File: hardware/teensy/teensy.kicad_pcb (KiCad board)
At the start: 2 copper layers, 215.9 x 152.4 mm, 99 parts, among them J4 CONN_083.5MM-8, J5 CONN_083.5MM-8, J6 CONN_083.5MM-8, J7 CONN_083.5MM-8, J8 CONN_023.5MM, J9 CONN_023.5MM

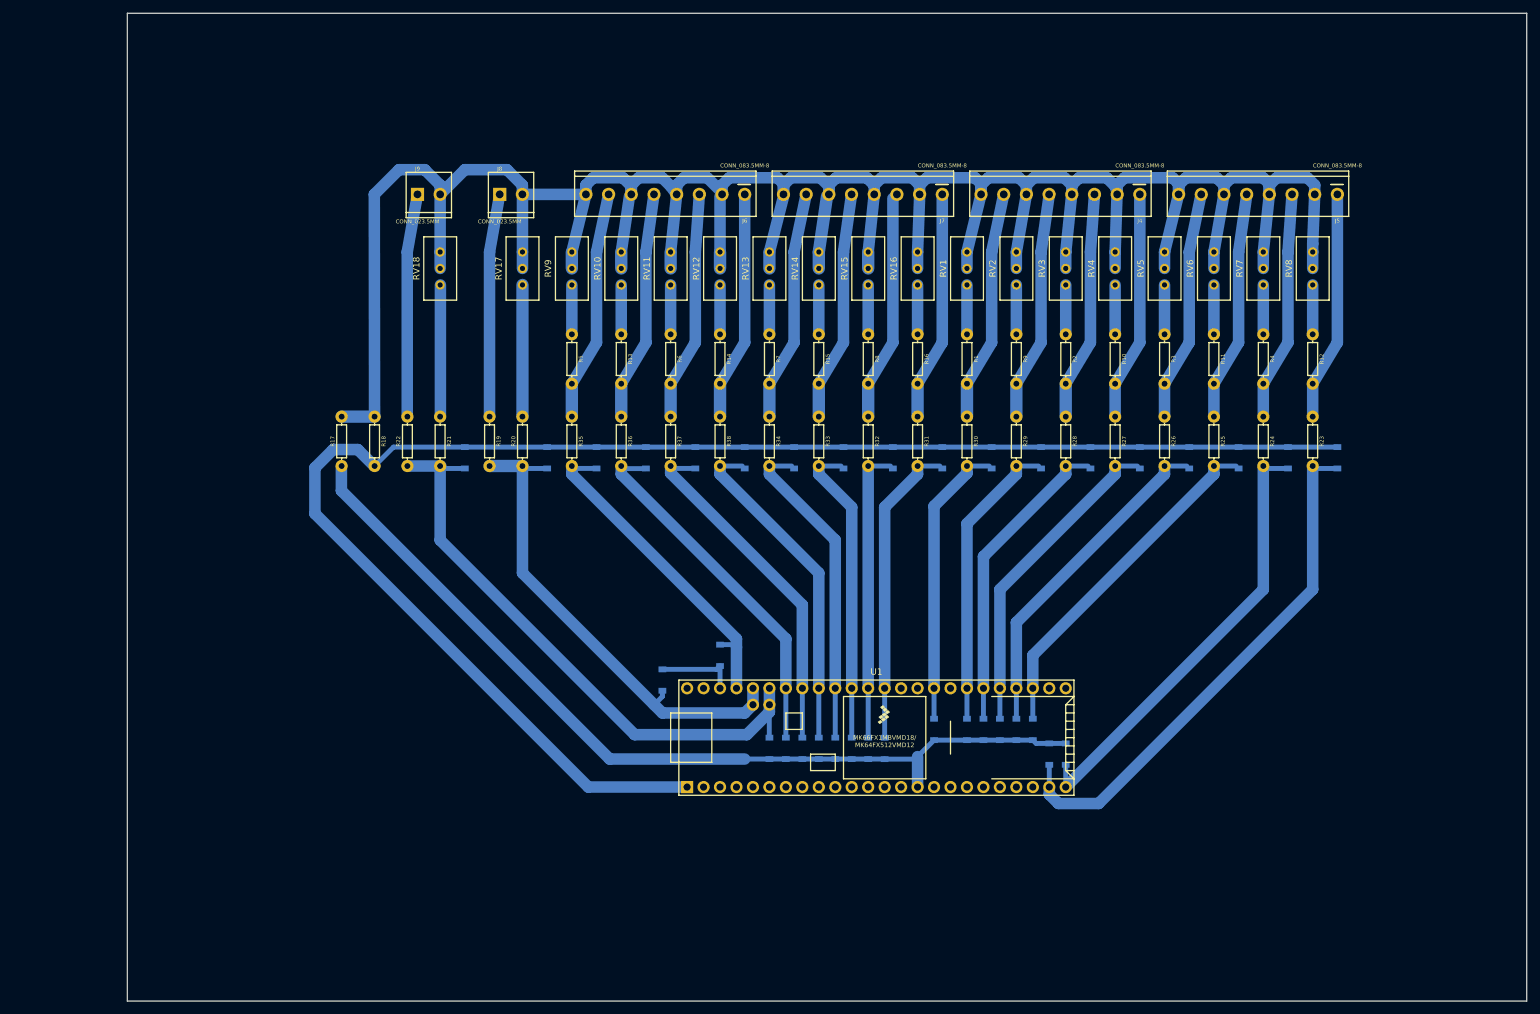
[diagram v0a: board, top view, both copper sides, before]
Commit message: got outline working
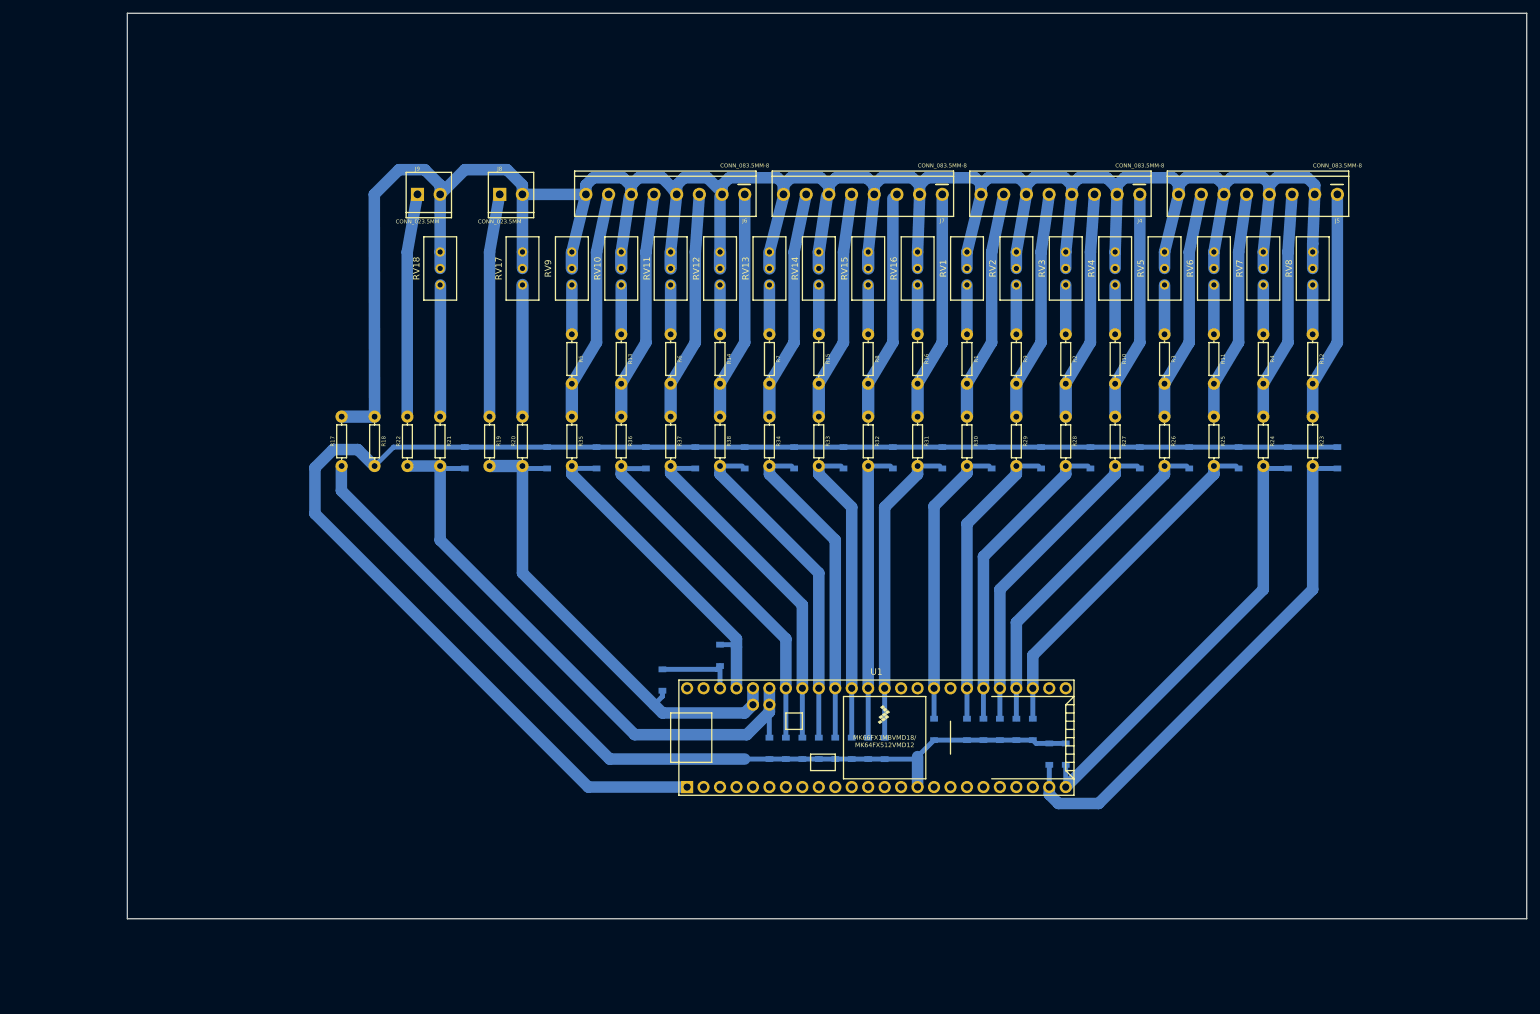
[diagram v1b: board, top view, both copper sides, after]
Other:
- board size 215.9 x 152.4 mm -> 215.9 x 139.7 mm
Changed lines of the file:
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@@
   (general
     (thickness 1.6)
-    (drawings 1)
+    (drawings 4)
     (tracks 348)
     (modules 99)
@@
       (sketchpadsonfab false)
       (subtractmaskfromsilk false)
-      (outputformat 3)
+      (outputformat 1)
       (mirror false)
       (drillshape 0)
@@
     )
   )
-  (gr_rect (start 38.1 25.4) (end 254 177.8) (layer "Edge.Cuts") (width 0.1))
+  (gr_line (start 254 25.4) (end 254 165.1) (layer "Edge.Cuts") (width 0.1))
+  (gr_line (start 38.1 25.4) (end 254 25.4) (layer "Edge.Cuts") (width 0.1))
+  (gr_line (start 38.1 165.1) (end 38.1 25.4) (layer "Edge.Cuts") (width 0.1))
+  (gr_line (start 254 165.1) (end 38.1 165.1) (layer "Edge.Cuts") (width 0.1))
   (segment (start 82.86242 53.34) (end 81.28 62.23) (width 1.778) (layer "B.Cu") (net 45))
   (segment (start 81.28 62.23) (end 81.28 87.602466) (width 1.778) (layer "B.Cu") (net 45))

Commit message: 2.54 rather than 3.5mm screws, now fits in 3x5
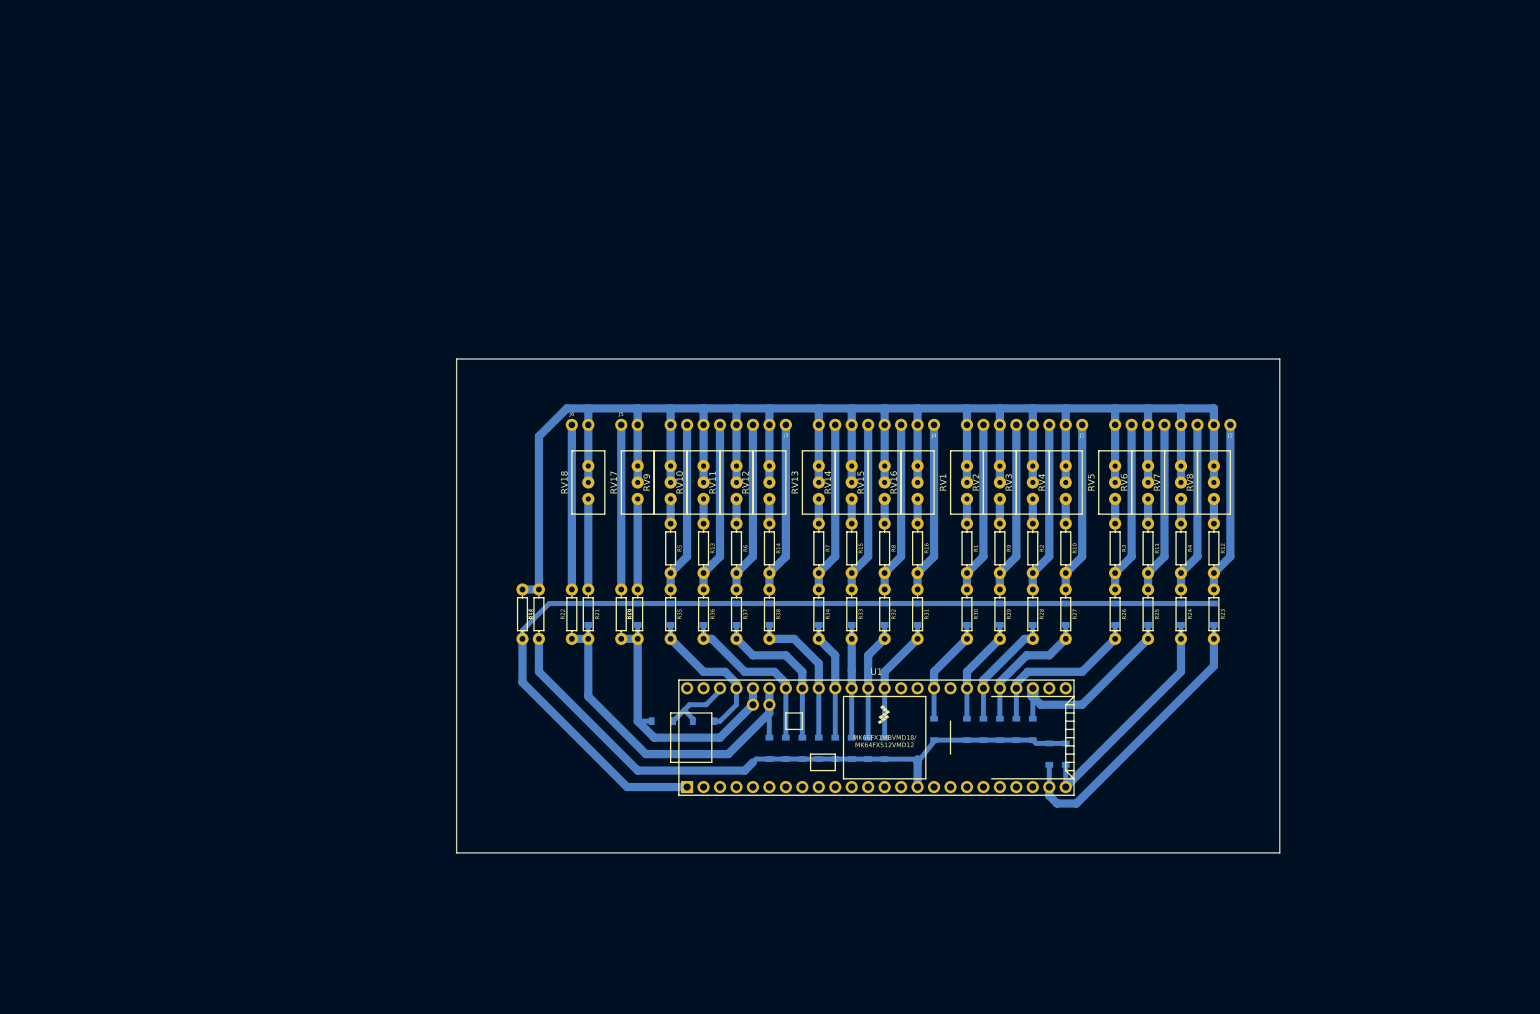
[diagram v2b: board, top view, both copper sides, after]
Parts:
- removed J7: CONN_083.5MM-8, Connectors:SCREWTERMINAL-3.5MM-8
- removed J8, J9: CONN_023.5MM, Connectors:SCREWTERMINAL-3.5MM-2
- added J1: CONN_08NO_SILK_FEMALE_PTH, Connectors:1X08_NO_SILK, F.Cu at (185.4, 88.9)
- added J2: CONN_08NO_SILK_FEMALE_PTH, Connectors:1X08_NO_SILK, F.Cu at (208.3, 88.9)
- added J3: CONN_08NO_SILK_FEMALE_PTH, Connectors:1X08_NO_SILK, F.Cu at (139.7, 88.9)
- J4: value CONN_083.5MM-8 -> CONN_08NO_SILK_FEMALE_PTH; footprint Connectors:SCREWTERMINAL-3.5MM-8 -> Connectors:1X08_NO_SILK
- J5, J6: value CONN_083.5MM-8 -> CONN_02; footprint Connectors:SCREWTERMINAL-3.5MM-8 -> Connectors:1X02_NO_SILK
- moved J5 116.1 mm to (114.3, 88.9), turned to 0 degrees
- moved J4 47.7 mm to (162.6, 88.9)
- moved J6 44.4 mm to (106.7, 88.9), turned to 0 degrees
- moved R17 40.5 mm to (101.6, 118.1)
- moved RV18 40.2 mm to (109.2, 95.2)
- moved RV17 37.5 mm to (116.8, 95.2)
- moved R22 36.8 mm to (106.7, 118.1)
- moved RV9 36.4 mm to (121.9, 95.2)
- moved RV8 36.4 mm to (205.7, 95.2)
- moved RV10 35.4 mm to (127.0, 95.2)
- moved RV7 35.4 mm to (200.7, 95.2)
- moved R21 35.1 mm to (109.2, 118.1)
- moved R18 35.1 mm to (99.1, 118.1)
- moved RV11 34.5 mm to (132.1, 95.2)
- moved RV6 34.5 mm to (195.6, 95.2)
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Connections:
- J4 pad 1: /ct13 -> /ct1
- J4 pad 3: /ct14 -> /ct2
- J4 pad 5: /ct15 -> /ct3
- J4 pad 7: /ct16 -> /ct4
- J5 pad 1: /ct9 -> /L2
- J6 pad 1: /ct5 -> /L1
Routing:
- net /CT_BIAS: track 445.6 -> 337.8 mm
- net /GND: track 243.1 -> 148.5 mm
- net /3.3V: track 138.7 -> 99.5 mm
- net /A11_A7: track 93.4 -> 55.4 mm
- net /A12: track 81.9 -> 45.9 mm
- net /A13: track 69.0 -> 35.9 mm
- net /A10_A8: track 75.3 -> 43.0 mm
- net /A3: track 49.5 -> 18.5 mm
- net /A2: track 47.4 -> 17.4 mm
- net /A6: track 55.8 -> 26.1 mm
- net /A5: track 53.8 -> 24.6 mm
- net /A4: track 51.7 -> 22.8 mm
- net /A19: track 47.7 -> 19.0 mm
- net /A18: track 49.8 -> 21.4 mm
- net /A20: track 45.6 -> 17.2 mm
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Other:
- board size 215.9 x 139.7 mm -> 127 x 76.2 mm

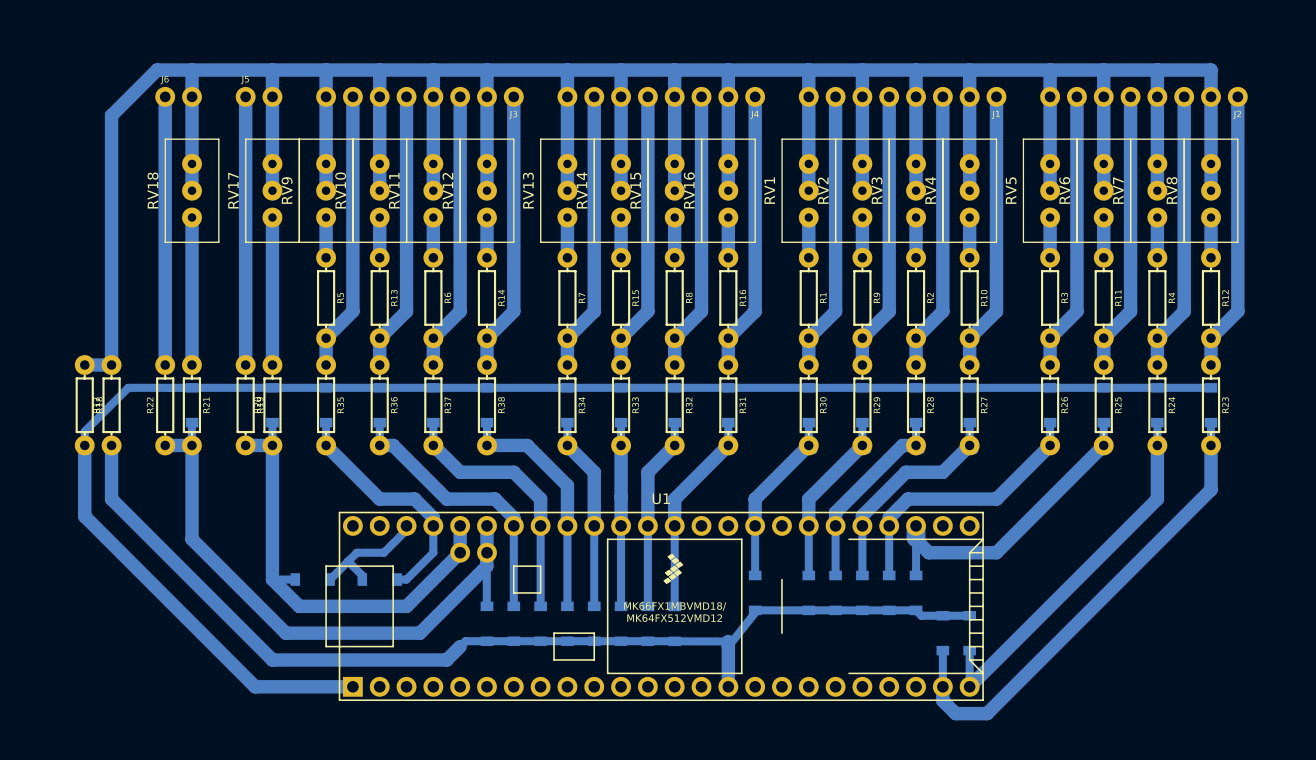
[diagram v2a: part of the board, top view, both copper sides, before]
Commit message: removed some resistors i don't need
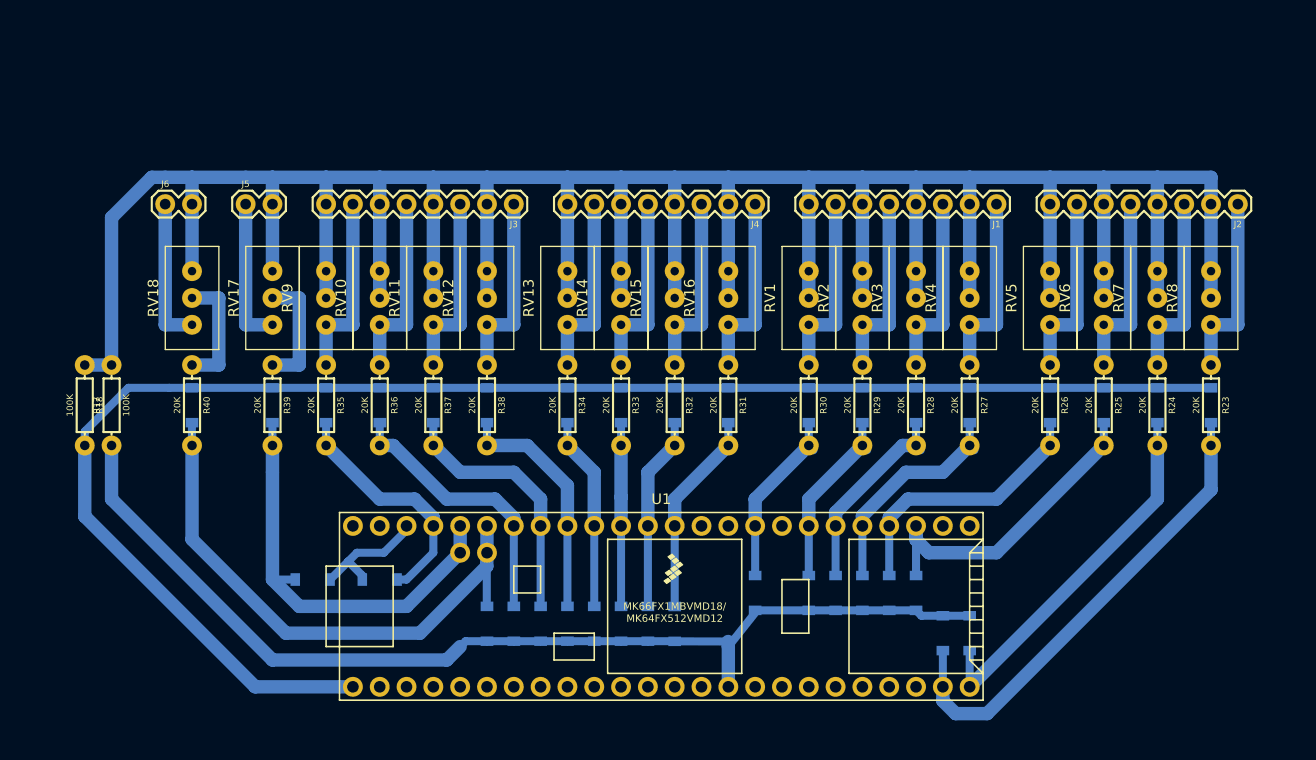
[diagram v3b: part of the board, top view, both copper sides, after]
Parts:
- removed R1, R10, R11, R12, R13, R14, R15, R16, R19, R2, R20, R21, R22, R3, R4, R5, R6, R7, R8, R9: ~, Resistors:AXIAL-0.3
- added R39: 20K, Resistors:AXIAL-0.3, F.Cu at (116.8, 118.1)
- added R40: 20K, Resistors:AXIAL-0.3, F.Cu at (109.2, 118.1)
- D1, D10, D11, D12, D13, D14, D15, D16, D17, D18, D19, D2, D20, D21, D22, D23, D24, D25, D26, D27, D28, D29, D3, D30, D31, D32, D33, D34, D35, D36, D4, D5, D6, D7, D8, D9: value D_Schottky -> ~
- J1, J2, J3, J4: value CONN_08NO_SILK_FEMALE_PTH -> ~; footprint Connectors:1X08_NO_SILK -> Connectors:1X08
- J5, J6: value CONN_02 -> ~; footprint Connectors:1X02_NO_SILK -> Connectors:1X02
- R17, R18: value ~ -> 100K
- R23, R24, R25, R26, R27, R28, R29, R30, R31, R32, R33, R34, R35, R36, R37, R38: value ~ -> 20K
- RV1, RV10, RV11, RV12, RV13, RV14, RV15, RV16, RV2, RV3, RV4, RV5, RV6, RV7, RV8, RV9: value R_POT_US -> 200
- RV17, RV18: value R_POT_US -> 100K
- U1: value ~ -> Teensy3.5
- moved J1 10.2 mm to (185.4, 99.1)
- moved J2 10.2 mm to (208.3, 99.1)
- moved J3 10.2 mm to (139.7, 99.1)
- moved J4 10.2 mm to (162.6, 99.1)
- moved J5 10.2 mm to (114.3, 99.1)
- moved J6 10.2 mm to (106.7, 99.1)
- moved RV1 10.2 mm to (167.6, 105.4)
- moved RV10 10.2 mm to (127.0, 105.4)
- moved RV11 10.2 mm to (132.1, 105.4)
- moved RV12 10.2 mm to (137.2, 105.4)
- moved RV13 10.2 mm to (144.8, 105.4)
- moved RV14 10.2 mm to (149.9, 105.4)
- moved RV15 10.2 mm to (154.9, 105.4)
- moved RV16 10.2 mm to (160.0, 105.4)
- moved RV17 10.2 mm to (116.8, 105.4)
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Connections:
- RV1 pad 3: Net-(R1-PadP$1) -> /ct16
- RV10 pad 3: Net-(R13-PadP$1) -> /ct7
- RV11 pad 3: Net-(R6-PadP$1) -> /ct6
- RV12 pad 3: Net-(R14-PadP$1) -> /ct5
- RV13 pad 3: Net-(R7-PadP$1) -> /ct4
- RV14 pad 3: Net-(R15-PadP$1) -> /ct3
- RV15 pad 3: Net-(R8-PadP$1) -> /ct2
- RV16 pad 3: Net-(R16-PadP$1) -> /ct1
- RV17 pad 2: /CT_BIAS -> /L2_SCALED
- RV17 pad 3: Net-(R20-PadP$2) -> /L2
- RV18 pad 2: /CT_BIAS -> /L1_SCALED
- RV18 pad 3: Net-(R21-PadP$1) -> /L1
- RV2 pad 3: Net-(R9-PadP$1) -> /ct15
- RV3 pad 3: Net-(R2-PadP$1) -> /ct14
- RV4 pad 3: Net-(R10-PadP$1) -> /ct13
- RV5 pad 3: Net-(R3-PadP$1) -> /ct12
- RV6 pad 3: Net-(R11-PadP$1) -> /ct11
- RV7 pad 3: Net-(R4-PadP$1) -> /ct10
- RV8 pad 3: Net-(R12-PadP$1) -> /ct9
- RV9 pad 3: Net-(R5-PadP$1) -> /ct8
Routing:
- net /CT_BIAS: track 337.8 -> 322.9 mm
- net Net-(R21-PadP$1): track 14.0 -> 0.00 mm
- net Net-(R20-PadP$2): track 14.0 -> 0.00 mm
- net /L1_SCALED: track 0.00 -> 11.4 mm
- net /L1: track 25.4 -> 14.0 mm
- net /L2: track 25.4 -> 14.0 mm
- net /L2_SCALED: track 0.00 -> 11.4 mm
- net /ct9: track 26.5 -> 17.8 mm
- net /ct8: track 26.5 -> 17.8 mm
- net /ct7: track 26.5 -> 17.8 mm
- net /ct6: track 26.5 -> 17.8 mm
- net /ct5: track 26.5 -> 17.8 mm
- net /ct4: track 26.5 -> 17.8 mm
- net /ct3: track 26.5 -> 17.8 mm
- net /ct2: track 26.5 -> 17.8 mm
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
